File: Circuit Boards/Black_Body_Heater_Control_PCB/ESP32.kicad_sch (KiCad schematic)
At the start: 24 parts, among them J201 5040500891, J202 Conn_01x04_Pin, J203 USB_C_Receptacle_USB2.0_16P, SW201 SW_MEC_5E, SW202 SW_MEC_5E, U201 AMS1117-3.3, U202 ESP32-S3-WROOM-1-N8R8, U203 USBLC6-2SC6

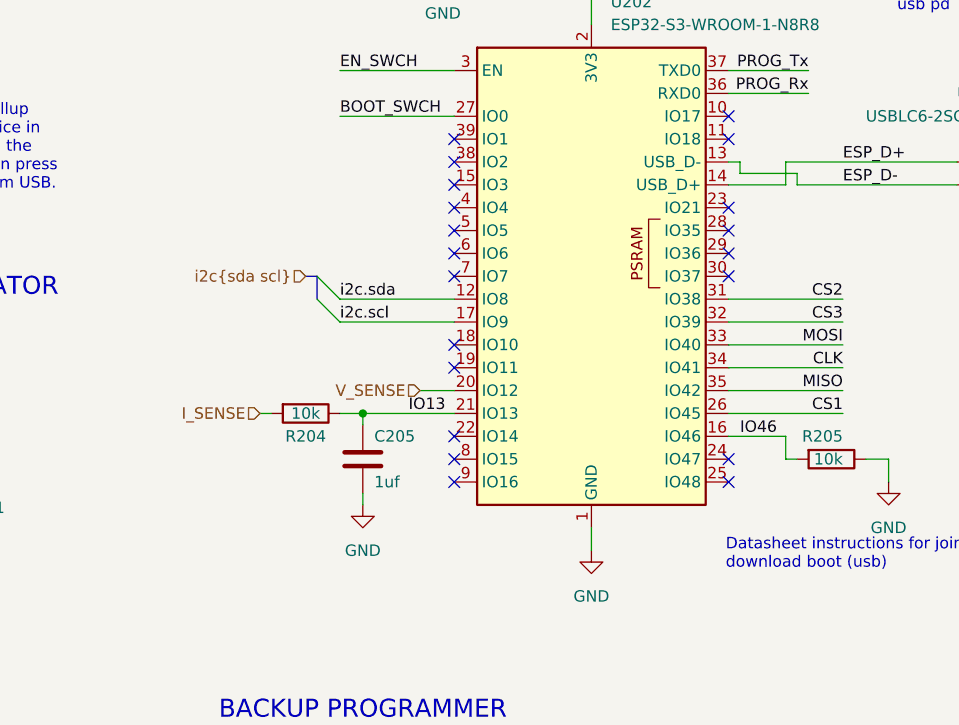
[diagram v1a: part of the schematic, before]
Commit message: Changing buck on heater pcb
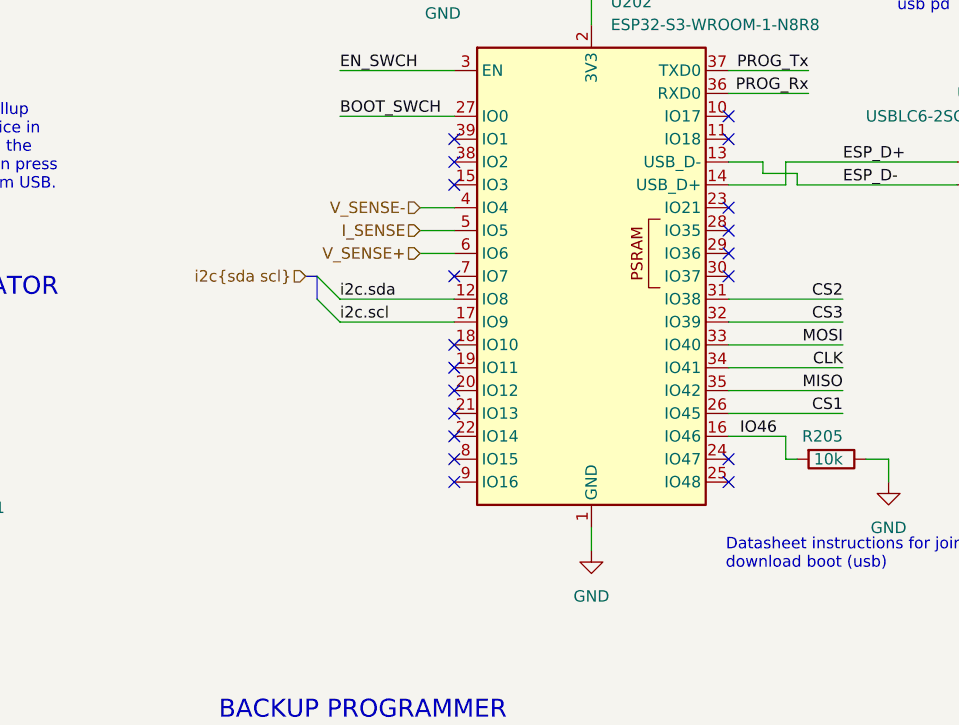
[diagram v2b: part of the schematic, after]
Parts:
- removed C205: 1uf, Capacitor_SMD:C_0603_1608Metric, symbol Device:C
- removed R204: 10k, Resistor_SMD:R_0603_1608Metric, symbol Device:R
- U202: footprint -mcu:ESP32-S3-WROOM-1 -> RF_Module:ESP32-S3-WROOM-1
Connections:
- net I_SENSE: now also U202.5 (IO5)
- net V_SENSE-: now reaches U202.4 (IO4)
- net V_SENSE+: now reaches U202.6 (IO6)
- net IO13: no longer names the net of U202.21 (IO13)
- net V_SENSE: no longer names the net of U202.20 (IO12)
- no-connect marks 27 -> 26
